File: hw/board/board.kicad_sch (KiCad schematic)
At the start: 7 parts, among them U1 XC7A35T-FTG256, U5 STM32F302CBTx, U6 W25Q128JVSIQTR

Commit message: Added reset + boot switches for STM32, re-routed power
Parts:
- removed U5: STM32F302CBTx, Package_QFP:LQFP-48_7x7mm_P0.5mm, symbol MCU_ST_STM32F3:STM32F302CBTx
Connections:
- no-connect marks 10 -> 119

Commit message: Added power connector, SWD/JTAG connectors
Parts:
- added H1, H2, H3, H4: MountingHole, MountingHole:MountingHole_2.2mm_M2, symbol Mechanical:MountingHole
- added J9: Conn_ARM_JTAG_SWD_10, Connector_PinHeader_1.27mm:PinHeader_2x05_P1.27mm_Vertical, symbol Connector:Conn_ARM_JTAG_SWD_10
- added R11: 0, Resistor_SMD:R_0805_2012Metric, symbol Device:R
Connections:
- net +2V5: now also R11.1
- net GND: now also J9.3 (GND), J9.5 (GND), J9.9 (GNDDetect)
- net TCK: now also J9.4 (SWCLK/TCK)
- net TDI: now also J9.8 (NC/TDI)
- net TDO: now also J9.6 (SWO/TDO)
- net TMS: now also J9.2 (SWDIO/TMS)
- new net: J9.1 (VTref), R11.2
- no-connect marks 119 -> 120

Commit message: Reannotated piece numbers
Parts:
- renumbered C15 to C1, C1 to C16, C17 to C2, H3 to H1, H4 to H3, H1 to H4, J9 to J2, R11 to R6, U6 to U2, U1 to U6
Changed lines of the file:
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@@
 		(dnp no)
 		(fields_autoplaced yes)
-		(property "Reference" "H3"
+		(property "Reference" "H1"
 			(at 53.34 49.5299 0)
 			(effects
@@
 			(project "board"
 				(path "/0e384709-6bce-4dbf-a0e0-550e970390f4"
-					(reference "H3")
+					(reference "H1")
 					(unit 1)
 				)
@@
 		(dnp no)
 		(fields_autoplaced yes)
-		(property "Reference" "J9"
+		(property "Reference" "J2"
 			(at 278.13 62.2299 0)
 			(effects
@@
 			(project "board"
 				(path "/0e384709-6bce-4dbf-a0e0-550e970390f4"
-					(reference "J9")
+					(reference "J2")
 					(unit 1)
 				)
@@
 		(on_board yes)
 		(dnp no)
-		(property "Reference" "C15"
+		(property "Reference" "C1"
 			(at 403.86 105.41 0)
 			(effects
@@
 			(project "board"
 				(path "/0e384709-6bce-4dbf-a0e0-550e970390f4"
-					(reference "C15")
+					(reference "C1")
 					(unit 1)
 				)
@@
 		(dnp no)
 		(fields_autoplaced yes)
-		(property "Reference" "U1"
+		(property "Reference" "U6"
 			(at 92.71 297.18 0)
 			(effects
@@
 			(project ""
 				(path "/0e384709-6bce-4dbf-a0e0-550e970390f4"
-					(reference "U1")
+					(reference "U6")
 					(unit 2)
 				)
@@
 		(dnp no)
 		(fields_autoplaced yes)
-		(property "Reference" "U1"
+		(property "Reference" "U6"
 			(at 384.81 297.18 0)
 			(effects
@@
 			(project ""
 				(path "/0e384709-6bce-4dbf-a0e0-550e970390f4"
-					(reference "U1")
+					(reference "U6")
 					(unit 1)
 				)
@@
 		(dnp no)
 		(fields_autoplaced yes)
-		(property "Reference" "H1"
+		(property "Reference" "H4"
 			(at 27.94 49.5299 0)
 			(effects
@@
 			(project "board"
 				(path "/0e384709-6bce-4dbf-a0e0-550e970390f4"
-					(reference "H1")
+					(reference "H4")
 					(unit 1)
 				)
@@
 		(dnp no)
 		(fields_autoplaced yes)
-		(property "Reference" "U6"
+		(property "Reference" "U2"
 			(at 368.3 93.98 0)
 			(effects
@@
 			(project ""
 				(path "/0e384709-6bce-4dbf-a0e0-550e970390f4"
-					(reference "U6")
+					(reference "U2")
 					(unit 1)
 				)
@@
 		(on_board yes)
 		(dnp no)
-		(property "Reference" "C17"
+		(property "Reference" "C2"
 			(at 414.02 105.41 0)
 			(effects
@@
 			(project "board"
 				(path "/0e384709-6bce-4dbf-a0e0-550e970390f4"
-					(reference "C17")
+					(reference "C2")
 					(unit 1)
 				)
@@
 		(dnp no)
 		(fields_autoplaced yes)
-		(property "Reference" "U1"
+		(property "Reference" "U6"
 			(at 125.73 74.2949 0)
 			(effects
@@
 			(project ""
 				(path "/0e384709-6bce-4dbf-a0e0-550e970390f4"
-					(reference "U1")
+					(reference "U6")
 					(unit 3)
 				)
@@
 		(dnp no)
 		(fields_autoplaced yes)
-		(property "Reference" "R11"
+		(property "Reference" "R6"
 			(at 292.1 40.6399 0)
 			(effects
@@
 			(project "board"
 				(path "/0e384709-6bce-4dbf-a0e0-550e970390f4"
-					(reference "R11")
+					(reference "R6")
 					(unit 1)
 				)
@@
 		(dnp no)
 		(fields_autoplaced yes)
-		(property "Reference" "H4"
+		(property "Reference" "H3"
 			(at 53.34 62.2299 0)
 			(effects
@@
 			(project "board"
 				(path "/0e384709-6bce-4dbf-a0e0-550e970390f4"
-					(reference "H4")
+					(reference "H3")
 					(unit 1)
 				)
@@
 		(on_board yes)
 		(dnp no)
-		(property "Reference" "C1"
+		(property "Reference" "C16"
 			(at 198.12 34.29 0)
 			(effects
@@
 			(project "board"
 				(path "/0e384709-6bce-4dbf-a0e0-550e970390f4"
-					(reference "C1")
+					(reference "C16")
 					(unit 1)
 				)

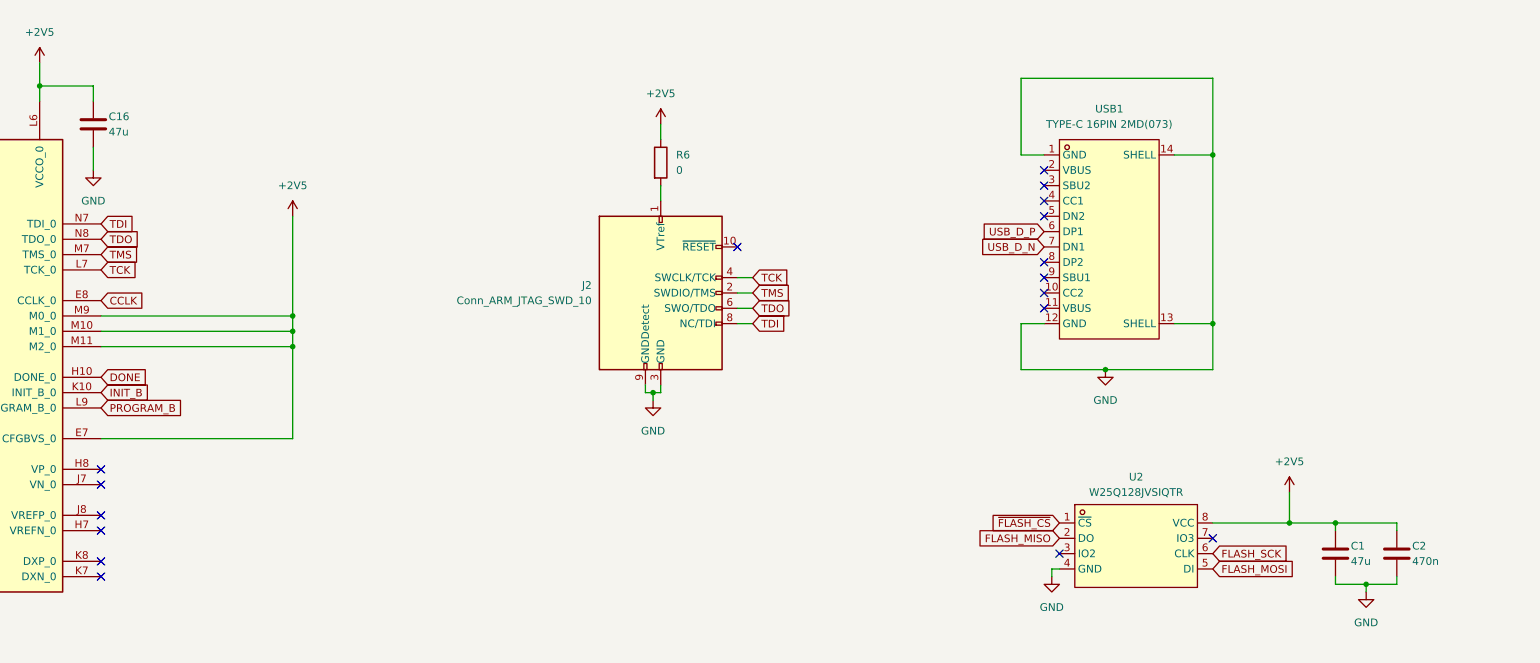
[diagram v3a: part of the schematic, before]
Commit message: Added capacitor for STM32 NRST
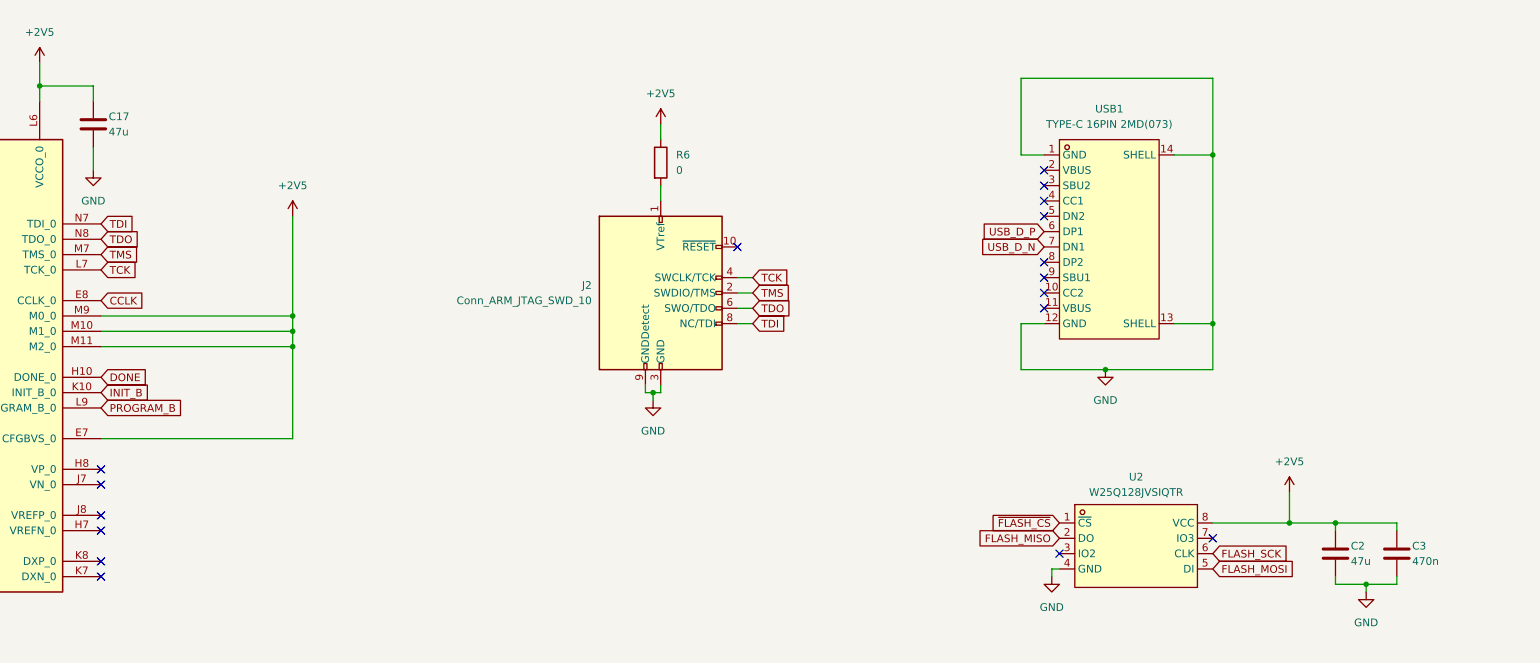
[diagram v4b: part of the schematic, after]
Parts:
- renumbered C16 to C17, C1 to C2, C2 to C3
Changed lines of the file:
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@@
 		(on_board yes)
 		(dnp no)
-		(property "Reference" "C1"
+		(property "Reference" "C2"
 			(at 403.86 105.41 0)
 			(effects
@@
 			(project "board"
 				(path "/0e384709-6bce-4dbf-a0e0-550e970390f4"
-					(reference "C1")
+					(reference "C2")
 					(unit 1)
 				)
@@
 		(on_board yes)
 		(dnp no)
-		(property "Reference" "C2"
+		(property "Reference" "C3"
 			(at 414.02 105.41 0)
 			(effects
@@
 			(project "board"
 				(path "/0e384709-6bce-4dbf-a0e0-550e970390f4"
-					(reference "C2")
+					(reference "C3")
 					(unit 1)
 				)
@@
 		(on_board yes)
 		(dnp no)
-		(property "Reference" "C16"
+		(property "Reference" "C17"
 			(at 198.12 34.29 0)
 			(effects
@@
 			(project "board"
 				(path "/0e384709-6bce-4dbf-a0e0-550e970390f4"
-					(reference "C16")
+					(reference "C17")
 					(unit 1)
 				)
